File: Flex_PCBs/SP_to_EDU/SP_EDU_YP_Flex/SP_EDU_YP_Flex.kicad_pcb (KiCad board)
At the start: 2 copper layers, 4.5 x 50 mm, 2 parts, among them J1 Conn_01x08_Male, J2 Conn_01x08_Male

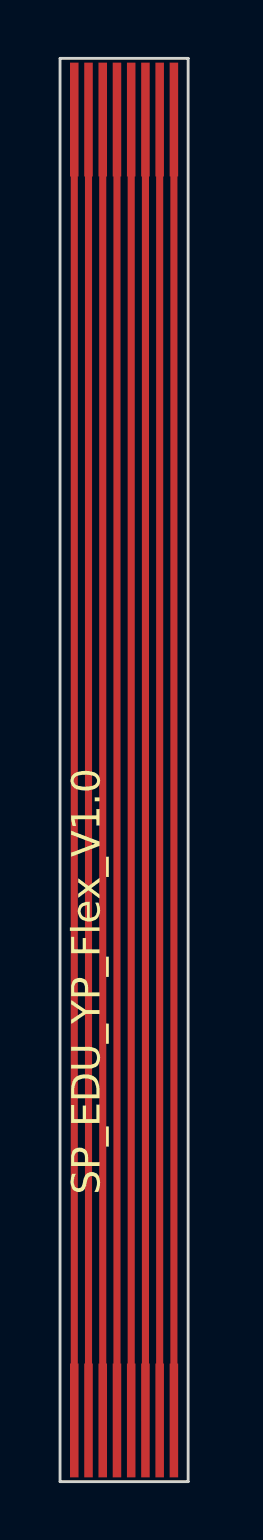
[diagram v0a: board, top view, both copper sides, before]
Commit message: replace ZF5S-*-01-T-WT and 2005280040 connectors with T1M-*-F-SH-L-FR connector
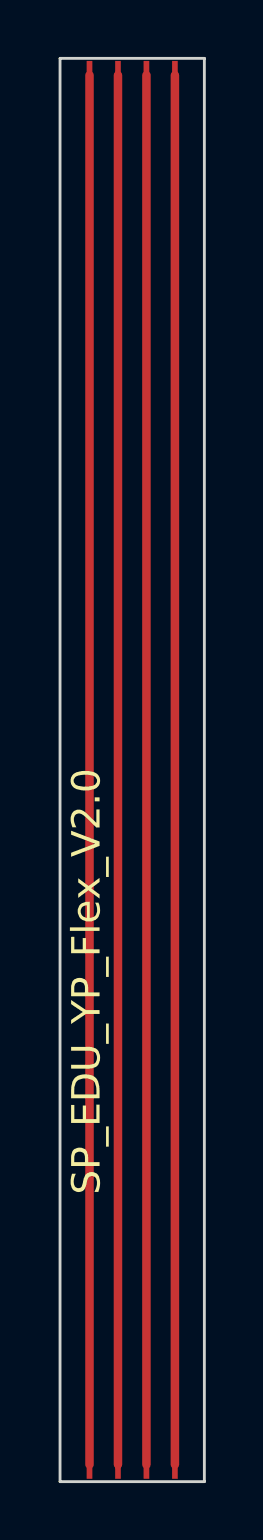
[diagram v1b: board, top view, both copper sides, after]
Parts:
- J1, J2: value Conn_01x08_Male -> Conn_01x04_Pin; footprint STS_connector:flexpcb con. -> STS_connector:flexPCB_connector_edu_sensors_new
- moved J2 5.00 mm to (123.5, 106.9), turned to 0 degrees
- moved J1 4.10 mm to (123.5, 58.1)
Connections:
- J1 pad 1: 8 -> 1
- J1 pad 2: 7 -> 2
- J1 pad 3: 6 -> 3
- J1 pad 4: 5 -> 4
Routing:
- net 8: track 45.7 -> 0.00 mm
- net 7: track 45.7 -> 0.00 mm
- net 6: track 45.7 -> 0.00 mm
- net 5: track 45.7 -> 0.00 mm
- net 4: track 45.7 -> 48.8 mm
- net 3: track 45.7 -> 48.8 mm
- net 2: track 45.7 -> 48.8 mm
- net 1: track 45.7 -> 48.8 mm
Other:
- board size 4.5 x 50 mm -> 5.1 x 50 mm
- board text added: "SP_EDU_YP_Flex_V2.0"
- board text removed: "SP_EDU_YP_Flex_V1.0"
